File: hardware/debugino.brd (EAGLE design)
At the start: 38.1 x 22.9 mm, 36 parts, among them Q1 12MHz, U2 ATMEGA328P-AU, U3 STM32F103CBT6, X1 MINI-USB-SCHIELD-32005-301

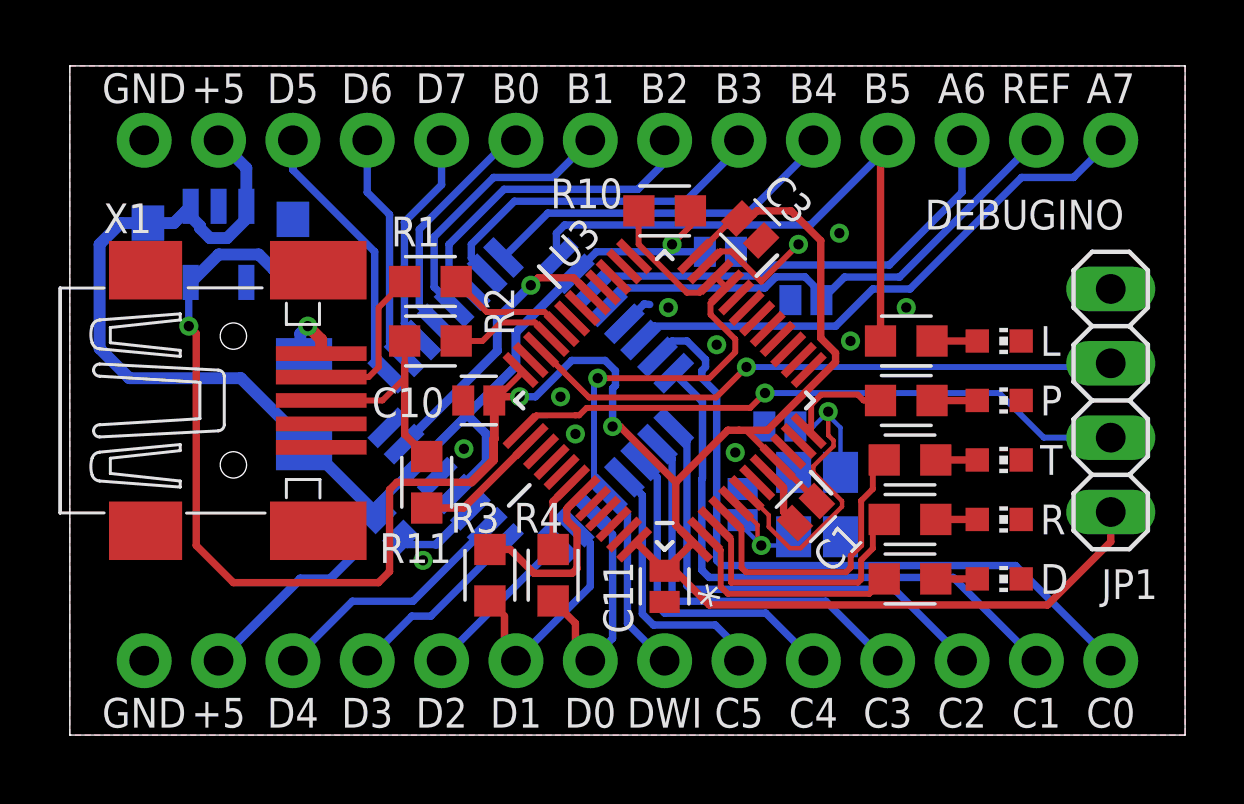
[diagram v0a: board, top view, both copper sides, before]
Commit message: Hardware for current measurement
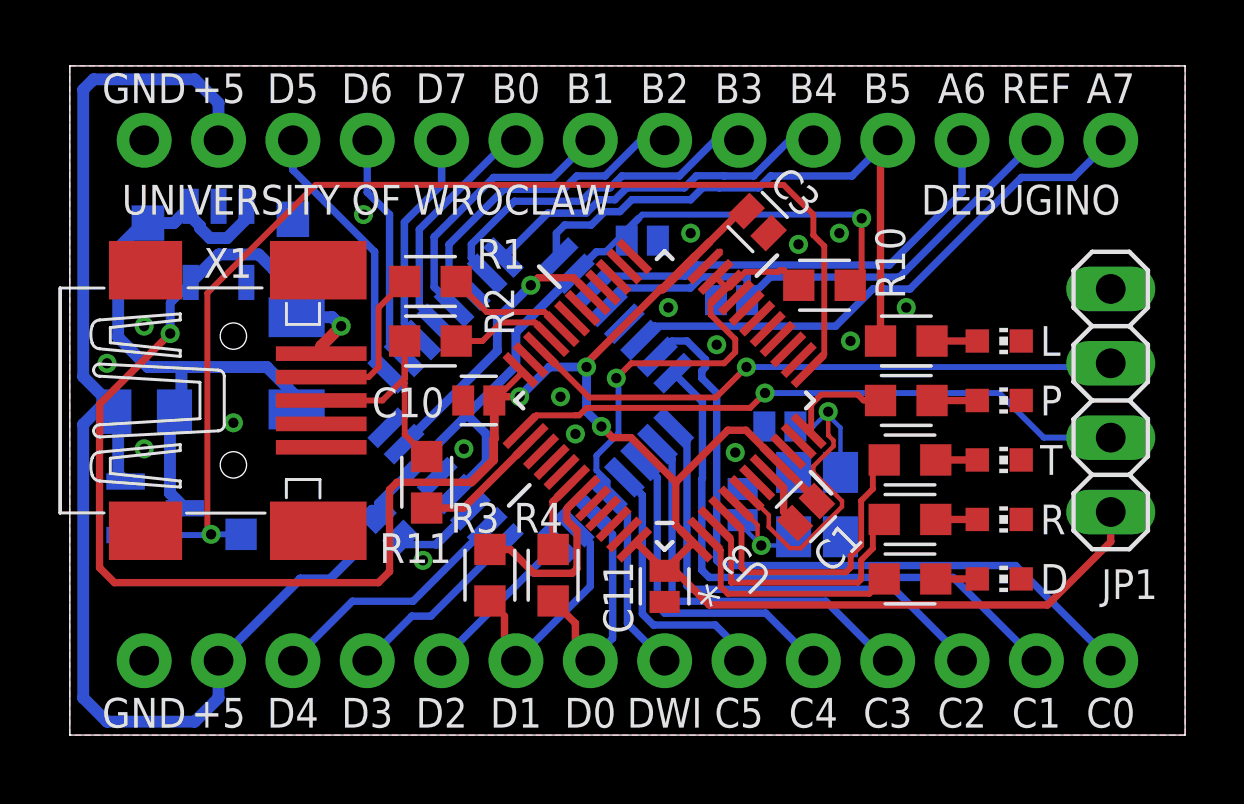
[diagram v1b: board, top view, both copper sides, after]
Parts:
- added R12: 0.47R, custom:RESC2012X65M
- added R13: 1K5, custom:RESC1608X55M
- added U1: ZXCT1107SA-7, Diodes_Inc_By_element14_Batch_1:SOT91P240X110-3N
- R3, R4: value 1K -> 1K5
- R5, R6, R7, R8, R9: value 1k -> 1K5
- moved R10 6.02 mm to (23.2, 15.4)
- moved C5 2.69 mm to (17.0, 16.9)
- moved C2 2.54 mm to (20.1, 14.9)
- moved F1 1.42 mm to (5.21, 12.7)
- moved C3 0.36 mm to (21.0, 17.5)
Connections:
- new net +5V: C5.2, C6.2, J1.13, J2.2, R10.2, R12.2, U1.2, U2.18, U2.4, U2.6
- new net CURRENT: R13.1, U1.1, U3.13
- net GND: now also R13.2
- net VCC: now also R12.1, U1.3; no longer C5.2, C6.2, J1.13, J2.2, R10.2, U2.18, U2.4, U2.6
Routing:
- net +5V: track 0.00 -> 74.4 mm, vias 0 -> 1
- net CURRENT: track 0.00 -> 40.6 mm, vias 0 -> 1
- net VCC: track 54.4 -> 21.9 mm, vias 1 -> 0
- net GND: track 10.8 -> 5.82 mm, vias 11 -> 17
- net !RESET: track 23.7 -> 21.6 mm
- net +3V3: track 84.0 -> 82.0 mm, vias 3 -> 4
- net N$5: track 2.35 -> 2.87 mm
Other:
- board text added: "UNIVERSITY OF WROCLAW"
